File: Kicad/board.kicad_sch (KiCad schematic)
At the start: 28 parts, among them SW1 SW_Push, SW10 SW_Push, SW11 SW_Push, SW12 SW_Push, SW13 RotaryEncoder, SW2 SW_Push, SW3 SW_Push, SW4 SW_Push, SW5 SW_Push, SW6 SW_Push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

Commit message: [add] add through hole
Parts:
- added H1, H2, H3, H4: MountingHole, MountingHole:MountingHole_2.7mm, symbol Mechanical:MountingHole
- D1, D10, D11, D12, D2, D3, D4, D5, D6, D7, D8, D9: footprint Diode_SMD:D_SOD-323 -> mylib:1n4148ws_reversible

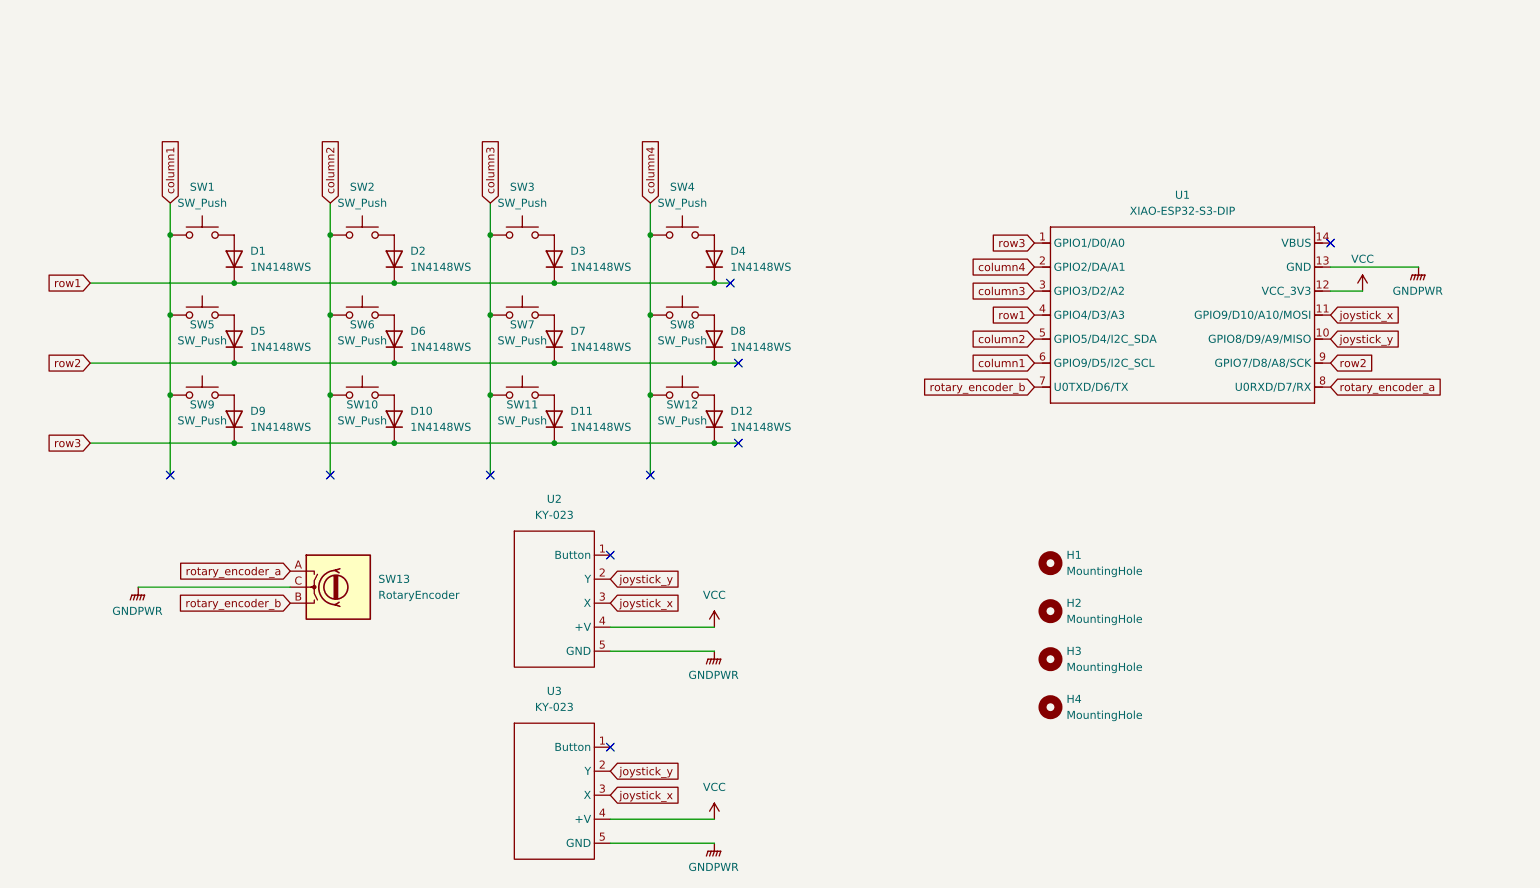
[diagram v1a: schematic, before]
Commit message: [add] add sign to silk layer
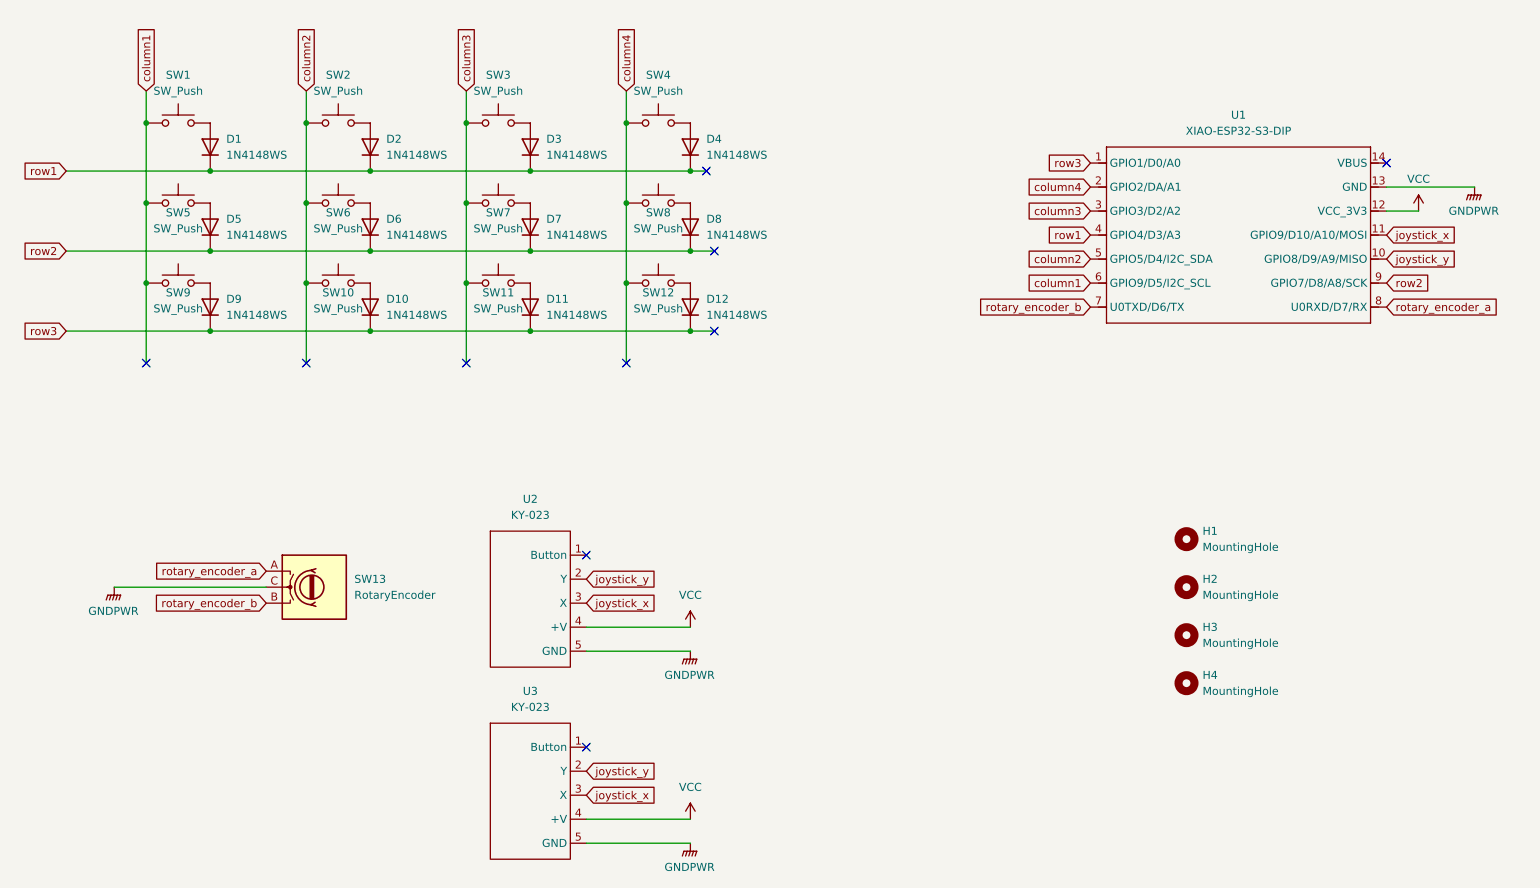
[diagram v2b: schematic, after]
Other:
- moved on the sheet: D1, D10, D11, D12, D2, D3, D4, D5, D6, D7, D8, D9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
